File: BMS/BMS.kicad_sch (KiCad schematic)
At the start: 23 parts, among them J1 USB4105-GF-A, J2 S70-125161545R, J3 S70-125161545R, J4 S70-125161545R, J5 S70-125161545R, J6 Conn_01x01, J7 Conn_01x01, U1 BQ29700DSER, U2 BQ25180YBGR, U3 CSD16406Q3, U4 TPD2E2U06DCKR, U5 CSD16406Q3

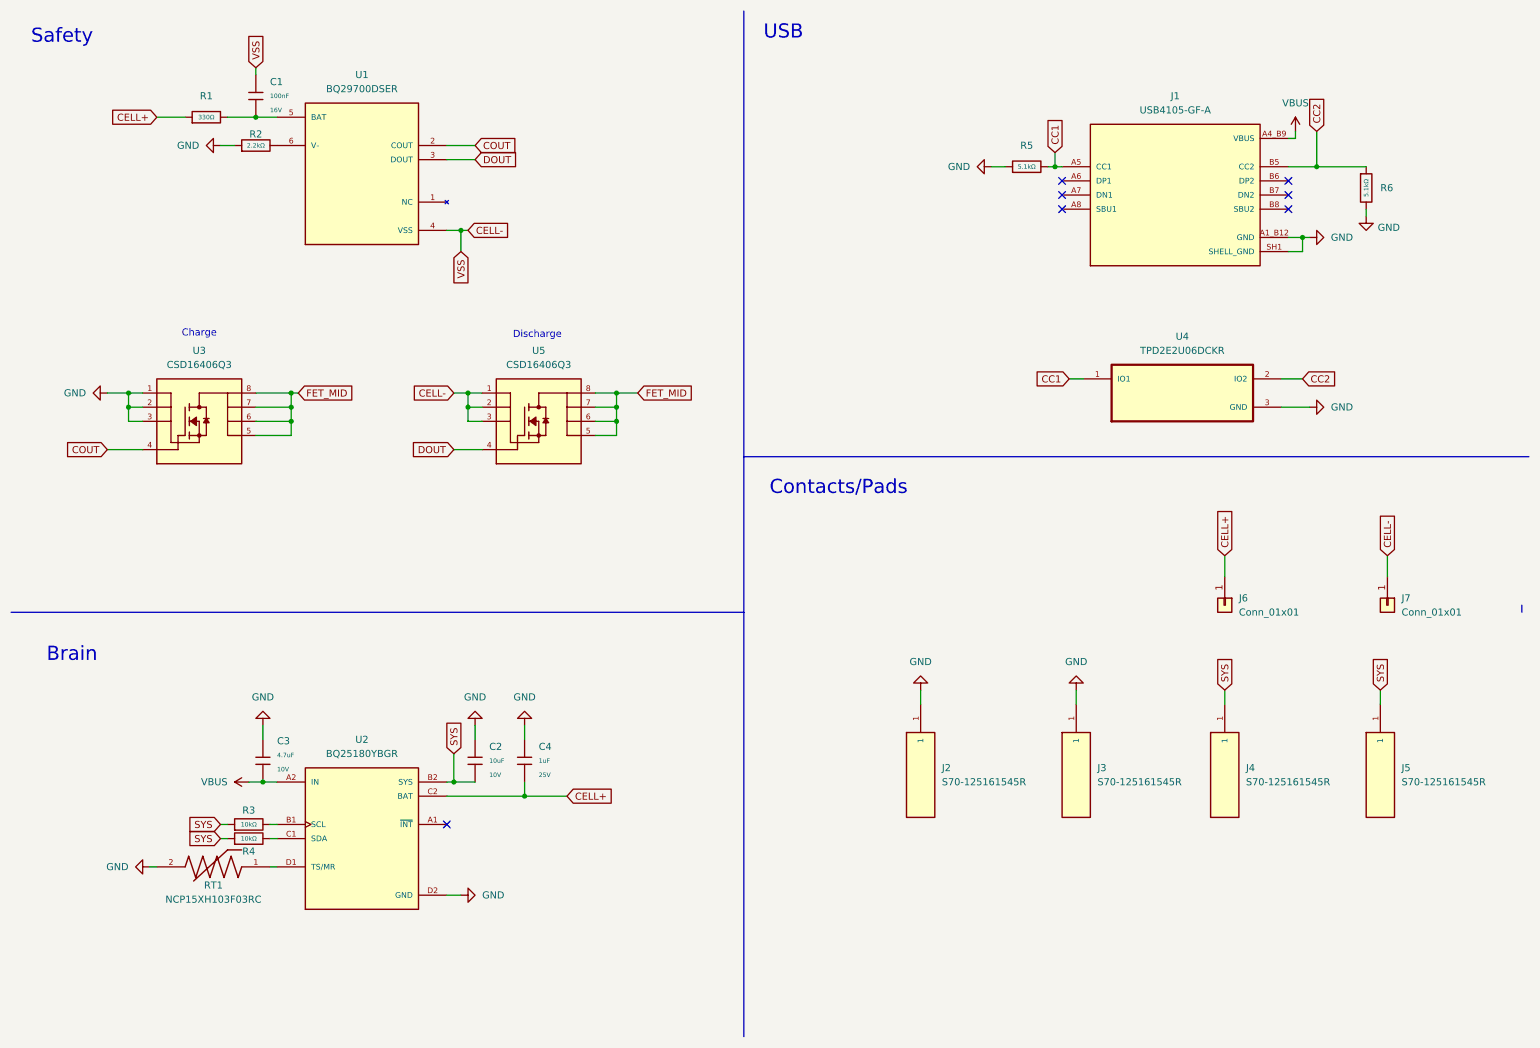
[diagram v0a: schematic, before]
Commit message: electronics: Sync latest designs from working directory
- Rename Puck board files (was Vent.kicad_* → Puck.kicad_*)
- Add full Comps libraries (footprints, models, symbols) for all four boards
- Add manufacturing-current/ Gerber outputs and renders for all boards
- Add new components: ESP32-C6-MINI-1 (Puck), ESP32-H2-MINI-1 (Vent), NCU15XH103F60RC (BMS)
- Add PCM JLCPCB passive symbol libraries across all boards
- Add per-project .gitignore files and Autoprogramming/AUTOPROGRAMMING_REVIEW.md
- Add root-level BOM files, sourcing audit, and manufacturing readiness ledger
- Update KiCad design files and Gerbers for BMS, Autoprogramming, and Vent

Co-Authored-By: Claude Sonnet 4.6 <noreply@anthropic.com>

Original-author: Zachariah K. Sharma <zachariah.sharma@gmail.com>
Source-commit: 261c676a3a26a8c60302274465dd756769088335
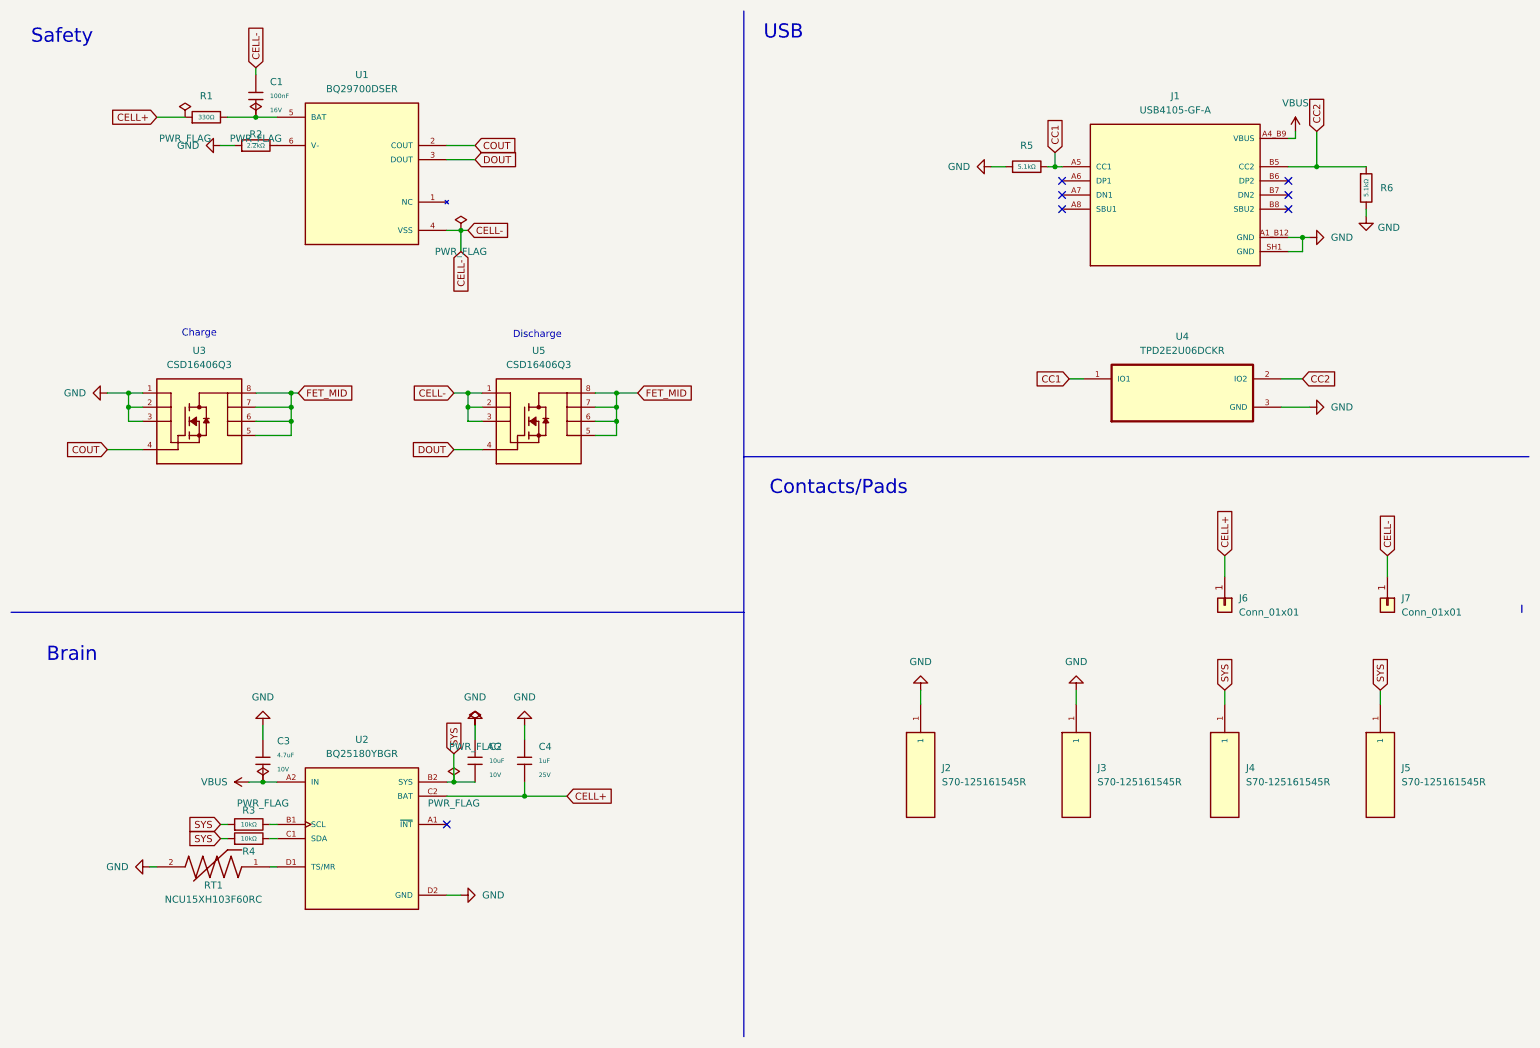
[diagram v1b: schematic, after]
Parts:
- RT1: value NCP15XH103F03RC -> NCU15XH103F60RC; symbol NCP15XH103F03RC:NCP15XH103F03RC -> NCU15XH103F60RC:NCU15XH103F60RC; Check_prices https://www.snapeda.com/parts/NCP15XH103F03RC/Murata/view-p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 -> https://www.digikey.com/en/products/detail/murata-electroni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; MP NCP15XH103F03RC -> NCU15XH103F60RC; SnapEDA_Link https://www.snapeda.com/parts/NCP15XH103F03RC/Murata/view-p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 -> https://www.digikey.com/en/products/detail/murata-electroni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
